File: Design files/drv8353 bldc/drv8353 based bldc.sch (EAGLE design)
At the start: 125 parts, among them IC1 DRV8353RSRGZT, J1 SSQ-110-01-G-D, J2 SSQ-110-01-G-D, J4 B06B-HCMKK

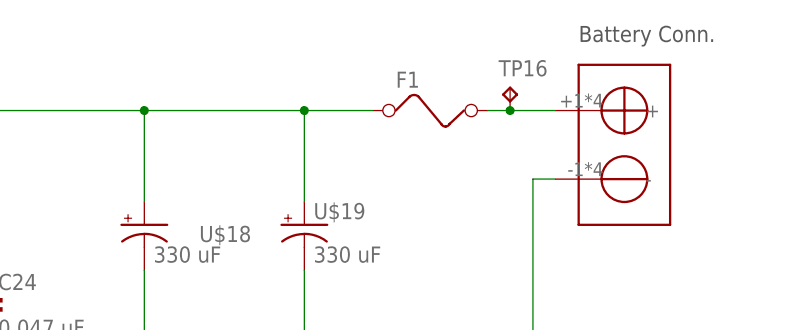
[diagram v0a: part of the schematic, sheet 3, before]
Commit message: replaced generic fuse with automotive style blade fuse
fuse chosen was the maxi standard becasue the regular ATO fuses max out at 40 amps and I'm not sure if that's enough for how we want to fuse this board
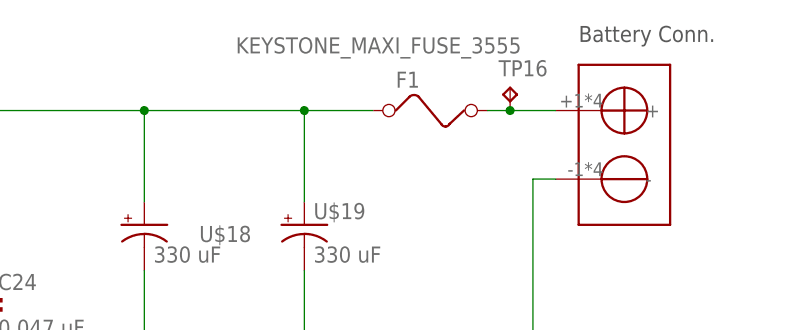
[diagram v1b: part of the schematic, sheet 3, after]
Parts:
- F1: value (none) -> KEYSTONE_MAXI_FUSE_3555; device special:FUSE -> REV BLDC:KEYSTONE_MAXI_FUSE_3555
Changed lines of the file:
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@@
 <part name="U$18" library="REV BLDC" deviceset="RADIALK16" device="" value="330 uF"/>
 <part name="U$19" library="REV BLDC" deviceset="RADIALK16" device="" value="330 uF"/>
-<part name="F1" library="special" library_urn="urn:adsk.eagle:library:367" deviceset="FUSE" device="" package3d_urn="urn:adsk.eagle:package:26650/1"/>
+<part name="F1" library="REV BLDC" deviceset="KEYSTONE_MAXI_FUSE_3555" device=""/>
 <part name="TP16" library="testpad" library_urn="urn:adsk.eagle:library:385" deviceset="TP" device="B1,27" package3d_urn="urn:adsk.eagle:package:27944/2"/>
 <part name="SUPPLY1" library="supply2" library_urn="urn:adsk.eagle:library:372" deviceset="GND" device=""/>
@@
 <instance part="F1" gate="G$1" x="60.96" y="71.12" smashed="yes">
 <attribute name="NAME" x="55.88" y="73.66" size="1.778" layer="95"/>
-<attribute name="VALUE" x="55.88" y="67.31" size="1.778" layer="96"/>
+<attribute name="VALUE" x="38.1" y="77.47" size="1.778" layer="96"/>
 </instance>
 <instance part="TP16" gate="G$1" x="68.58" y="73.66" smashed="yes">

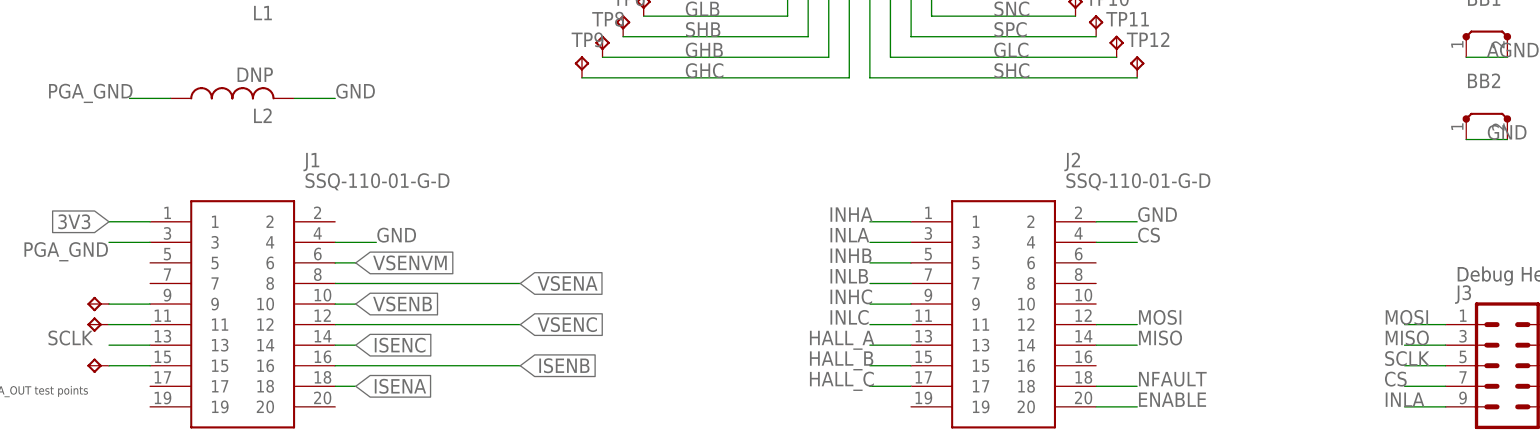
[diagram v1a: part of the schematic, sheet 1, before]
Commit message: created communications boards, combined 2x10 headers
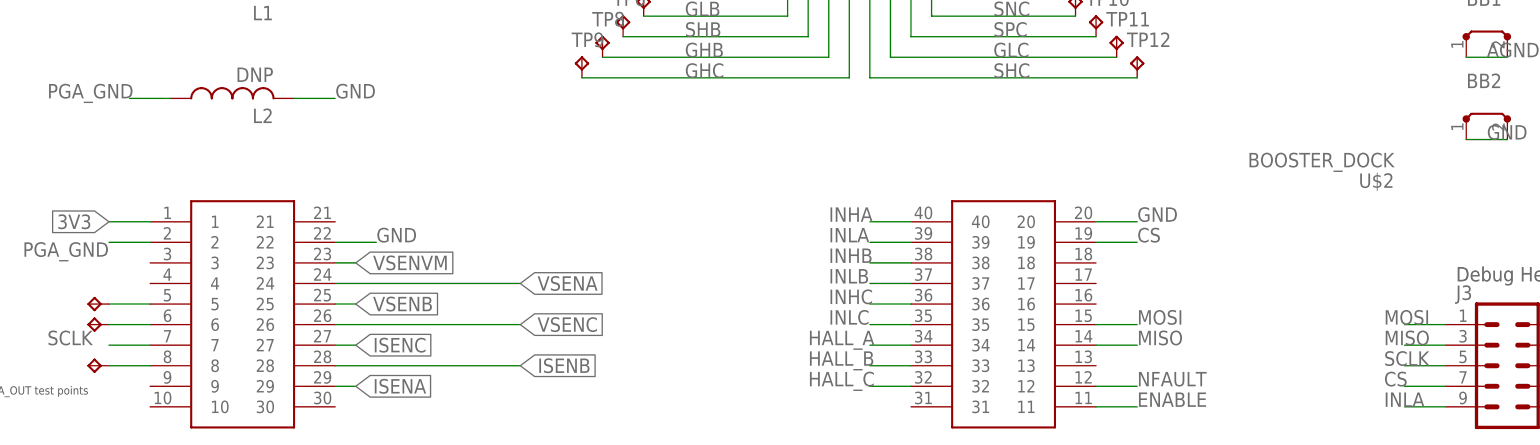
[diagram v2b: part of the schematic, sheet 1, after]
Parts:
- removed J1, J2: SSQ-110-01-G-D, SamacSys_Parts:SSQ-110-01-G-D
- added U$2: BOOSTER_DOCK, REV BLDC:BOOSTER_DOCK
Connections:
- net 3V3: now also U$2.1; no longer J1.1
- net CS: now also U$2.19; no longer J2.4
- net ENABLE: now also U$2.11; no longer J2.20
- net GND: now also U$2.20, U$2.22; no longer J1.4, J2.2
- net HALL_A: now also U$2.34; no longer J2.13
- net HALL_B: now also U$2.33; no longer J2.15
- net HALL_C: now also U$2.32; no longer J2.17
- net INHA: now also U$2.40; no longer J2.1
- net INHB: now also U$2.38; no longer J2.5
- net INHC: now also U$2.36; no longer J2.9
- net INLA: now also U$2.39; no longer J2.3
- net INLB: now also U$2.37; no longer J2.7
- net INLC: now also U$2.35; no longer J2.11
- net ISENA: now also U$2.29; no longer J1.18
- net ISENB: now also U$2.28; no longer J1.16
- net ISENC: now also U$2.27; no longer J1.14
- net MISO: now also U$2.14; no longer J2.14
- net MOSI: now also U$2.15; no longer J2.12
- net N$17: now also U$2.8; no longer J1.15
- net N$18: now also U$2.6; no longer J1.11
- net N$19: now also U$2.5; no longer J1.9
- net NFAULT: now also U$2.12; no longer J2.18
- net PGA_GND: now also U$2.2; no longer J1.3
- net SCLK: now also U$2.7; no longer J1.13
- net VSENA: now also U$2.24; no longer J1.8
- net VSENB: now also U$2.25; no longer J1.10
- net VSENC: now also U$2.26; no longer J1.12
- net VSENVM: now also U$2.23; no longer J1.6

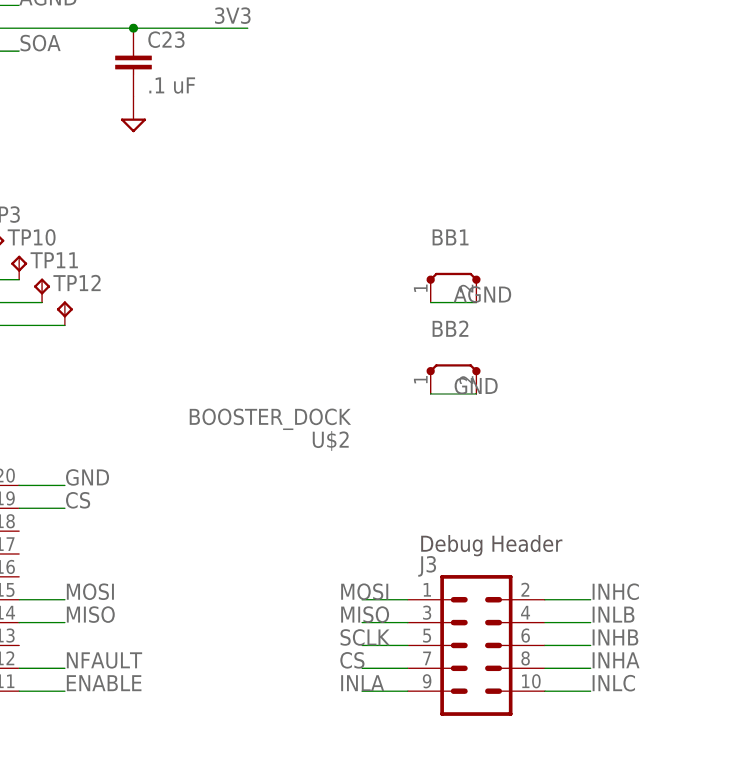
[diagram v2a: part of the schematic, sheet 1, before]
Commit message: adds power switch to motor controller
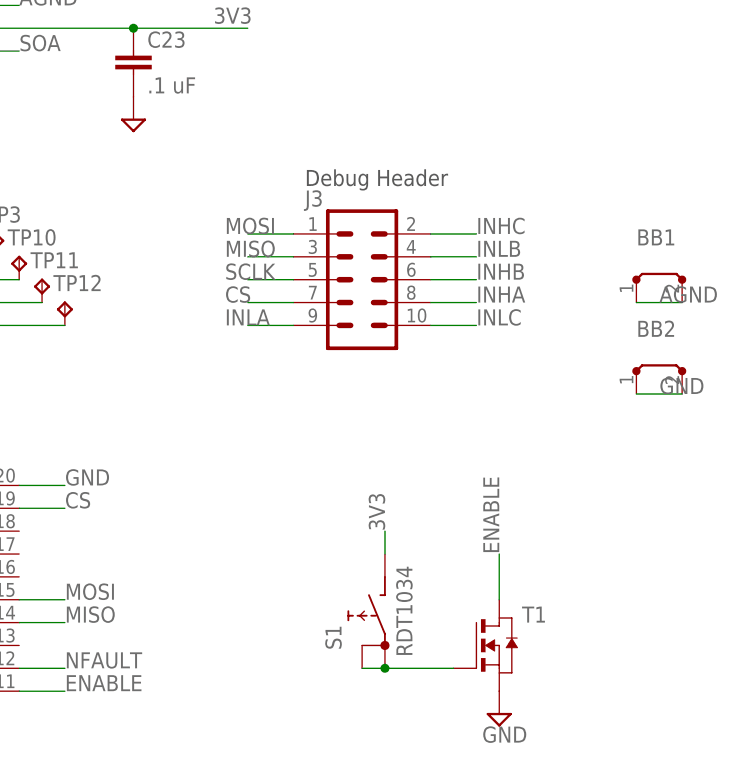
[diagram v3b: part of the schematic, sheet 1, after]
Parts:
- added S1: RDT1034, switch:RDT1034
- added T1: (no value), zetex:NMOSSOT23
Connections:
- new net N$20: S1.A, S1.A1, T1.G
- net 3V3: now also S1.B
- net ENABLE: now also T1.D
- net GND: now also T1.S
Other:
- moved on the sheet: BB1, BB2, J3
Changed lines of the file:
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@@
 <?xml version="1.0" encoding="utf-8"?>
 <!DOCTYPE eagle SYSTEM "eagle.dtd">
-<eagle version="9.5.0">
+<eagle version="9.5.1">
 <drawing>
 <settings>
@@
 <part name="J4" library="SamacSys_Parts" deviceset="B06B-HCMKK" device=""/>
 <part name="U$2" library="REV BLDC" deviceset="BOOSTER_DOCK" device=""/>
+<part name="S1" library="switch" library_urn="urn:adsk.eagle:library:380" deviceset="RDT1034" device="" package3d_urn="urn:adsk.eagle:package:27704/1"/>
+<part name="T1" library="zetex" library_urn="urn:adsk.eagle:library:418" deviceset="NMOSSOT23" device="" package3d_urn="urn:adsk.eagle:package:30981/1"/>
+<part name="SUPPLY10" library="supply2" library_urn="urn:adsk.eagle:library:372" deviceset="GND" device=""/>
 </parts>
 <sheets>
@@
 <plain>
 <frame x1="-96.52" y1="-154.94" x2="134.62" y2="33.02" columns="8" rows="5" layer="97"/>
-<text x="92.71" y="-124.206" size="1.778" layer="97">Debug Header</text>
+<text x="80.01" y="-83.566" size="1.778" layer="97">Debug Header</text>
 <text x="-76.2" y="-137.16" size="1.016" layer="97" rot="R180">PGA_OUT test points</text>
 <text x="-66.04" y="-86.36" size="1.778" layer="97">Ferrite Bead</text>
@@
 <attribute name="TP_SIGNAL_NAME" x="-3.81" y="-59.69" size="1.778" layer="97" rot="R180"/>
 </instance>
-<instance part="J3" gate="G$1" x="99.06" y="-134.62" smashed="yes">
-<attribute name="VALUE" x="95.25" y="-144.526" size="1.778" layer="96" font="vector"/>
-<attribute name="NAME" x="92.71" y="-126.492" size="1.778" layer="95" font="vector"/>
+<instance part="J3" gate="G$1" x="86.36" y="-93.98" smashed="yes">
+<attribute name="VALUE" x="82.55" y="-103.886" size="1.778" layer="96" font="vector"/>
+<attribute name="NAME" x="80.01" y="-85.852" size="1.778" layer="95" font="vector"/>
 </instance>
 <instance part="L2" gate="G$1" x="-58.42" y="-101.6" smashed="yes" rot="R90">
@@
 <attribute name="VALUE" x="-53.34" y="-85.09" size="1.778" layer="96" rot="R180"/>
 </instance>
-<instance part="BB1" gate="1" x="96.52" y="-93.98" smashed="yes">
-<attribute name="NAME" x="93.98" y="-90.17" size="1.778" layer="95"/>
-<attribute name="VALUE" x="93.98" y="-92.71" size="1.778" layer="96"/>
-</instance>
-<instance part="BB2" gate="1" x="96.52" y="-104.14" smashed="yes">
-<attribute name="NAME" x="93.98" y="-100.33" size="1.778" layer="95"/>
-<attribute name="VALUE" x="93.98" y="-102.87" size="1.778" layer="96"/>
-</instance>
-<instance part="U$2" gate="G$1" x="-68.58" y="-116.84" smashed="yes">
-<attribute name="NAME" x="-49.53" y="-109.22" size="1.778" layer="95" align="center-left"/>
-<attribute name="VALUE" x="-49.53" y="-111.76" size="1.778" layer="96" align="center-left"/>
-<attribute name="NAME" x="85.09" y="-111.76" size="1.778" layer="95" rot="R180" align="center-left"/>
-<attribute name="VALUE" x="85.09" y="-109.22" size="1.778" layer="96" rot="R180" align="center-left"/>
+<instance part="BB1" gate="1" x="119.38" y="-93.98" smashed="yes">
+<attribute name="NAME" x="116.84" y="-90.17" size="1.778" layer="95"/>
+<attribute name="VALUE" x="116.84" y="-92.71" size="1.778" layer="96"/>
+</instance>
+<instance part="BB2" gate="1" x="119.38" y="-104.14" smashed="yes">
+<attribute name="NAME" x="116.84" y="-100.33" size="1.778" layer="95"/>
+<attribute name="VALUE" x="116.84" y="-102.87" size="1.778" layer="96"/>
+</instance>
+<instance part="U$2" gate="G$1" x="-68.58" y="-116.84" smashed="yes"/>
+<instance part="S1" gate="G$1" x="86.36" y="-132.08" smashed="yes" rot="R90">
+<attribute name="NAME" x="84.074" y="-135.128" size="1.778" layer="95" rot="R90"/>
+<attribute name="VALUE" x="91.948" y="-135.89" size="1.778" layer="96" rot="R90"/>
+</instance>
+<instance part="T1" gate="A" x="101.6" y="-134.62" smashed="yes">
+<attribute name="VALUE" x="104.14" y="-134.62" size="1.778" layer="96"/>
+<attribute name="NAME" x="104.14" y="-132.08" size="1.778" layer="95"/>
+</instance>
+<instance part="SUPPLY10" gate="GND" x="101.6" y="-142.24" smashed="yes">
+<attribute name="VALUE" x="99.695" y="-145.415" size="1.778" layer="96"/>
 </instance>
 </instances>
@@
 <pinref part="BB2" gate="1" pin="P@1"/>
 <pinref part="BB2" gate="1" pin="P@2"/>
-<wire x1="93.98" y1="-106.68" x2="99.06" y2="-106.68" width="0.1524" layer="91"/>
-<label x="96.52" y="-106.68" size="1.778" layer="95"/>
+<wire x1="116.84" y1="-106.68" x2="121.92" y2="-106.68" width="0.1524" layer="91"/>
+<label x="119.38" y="-106.68" size="1.778" layer="95"/>
 </segment>
 <segment>
@@
 <label x="53.34" y="-116.84" size="1.778" layer="95"/>
 <pinref part="U$2" gate="G$1" pin="20"/>
+</segment>
+<segment>
+<pinref part="T1" gate="A" pin="S"/>
+<pinref part="SUPPLY10" gate="GND" pin="GND"/>
 </segment>
 </net>
@@
 <segment>
 <pinref part="J3" gate="G$1" pin="4"/>
-<wire x1="106.68" y1="-132.08" x2="111.76" y2="-132.08" width="0.1524" layer="91"/>
-<label x="111.76" y="-132.08" size="1.778" layer="95"/>
+<wire x1="93.98" y1="-91.44" x2="99.06" y2="-91.44" width="0.1524" layer="91"/>
+<label x="99.06" y="-91.44" size="1.778" layer="95"/>
 </segment>
 </net>
@@
 <segment>
 <pinref part="J3" gate="G$1" pin="2"/>
-<wire x1="106.68" y1="-129.54" x2="111.76" y2="-129.54" width="0.1524" layer="91"/>
-<label x="111.76" y="-129.54" size="1.778" layer="95"/>
+<wire x1="93.98" y1="-88.9" x2="99.06" y2="-88.9" width="0.1524" layer="91"/>
+<label x="99.06" y="-88.9" size="1.778" layer="95"/>
 </segment>
 </net>
@@
 <segment>
 <pinref part="J3" gate="G$1" pin="10"/>
-<wire x1="106.68" y1="-139.7" x2="111.76" y2="-139.7" width="0.1524" layer="91"/>
-<label x="111.76" y="-139.7" size="1.778" layer="95"/>
+<wire x1="93.98" y1="-99.06" x2="99.06" y2="-99.06" width="0.1524" layer="91"/>
+<label x="99.06" y="-99.06" size="1.778" layer="95"/>
 </segment>
 </net>
@@
 <segment>
 <pinref part="J3" gate="G$1" pin="6"/>
-<wire x1="106.68" y1="-134.62" x2="111.76" y2="-134.62" width="0.1524" layer="91"/>
-<label x="111.76" y="-134.62" size="1.778" layer="95"/>
+<wire x1="93.98" y1="-93.98" x2="99.06" y2="-93.98" width="0.1524" layer="91"/>
+<label x="99.06" y="-93.98" size="1.778" layer="95"/>
 </segment>
 </net>
@@
 <segment>
 <pinref part="J3" gate="G$1" pin="9"/>
-<wire x1="91.44" y1="-139.7" x2="86.36" y2="-139.7" width="0.1524" layer="91"/>
-<label x="83.82" y="-139.7" size="1.778" layer="95"/>
+<wire x1="78.74" y1="-99.06" x2="73.66" y2="-99.06" width="0.1524" layer="91"/>
+<label x="71.12" y="-99.06" size="1.778" layer="95"/>
 </segment>
 </net>
@@
 <segment>
 <pinref part="J3" gate="G$1" pin="8"/>
-<wire x1="106.68" y1="-137.16" x2="111.76" y2="-137.16" width="0.1524" layer="91"/>
-<label x="111.76" y="-137.16" size="1.778" layer="95"/>
+<wire x1="93.98" y1="-96.52" x2="99.06" y2="-96.52" width="0.1524" layer="91"/>
+<label x="99.06" y="-96.52" size="1.778" layer="95"/>
 </segment>
 </net>
@@
 <pinref part="U$2" gate="G$1" pin="1"/>
 </segment>
+<segment>
+<pinref part="S1" gate="G$1" pin="B"/>
+<wire x1="88.9" y1="-124.46" x2="88.9" y2="-121.92" width="0.1524" layer="91"/>
+<label x="88.9" y="-121.92" size="1.778" layer="95" rot="R90"/>
+</segment>
 </net>
 <net name="ENABLE" class="0">
@@
 <pinref part="U$2" gate="G$1" pin="11"/>
 </segment>
+<segment>
+<pinref part="T1" gate="A" pin="D"/>
+<wire x1="101.6" y1="-129.54" x2="101.6" y2="-124.46" width="0.1524" layer="91"/>
+<label x="101.6" y="-124.46" size="1.778" layer="95" rot="R90"/>
+</segment>
 </net>
 <net name="CS" class="0">
@@
 <segment>
 <pinref part="J3" gate="G$1" pin="7"/>
-<wire x1="91.44" y1="-137.16" x2="86.36" y2="-137.16" width="0.1524" layer="91"/>
-<label x="83.82" y="-137.16" size="1.778" layer="95"/>
+<wire x1="78.74" y1="-96.52" x2="73.66" y2="-96.52" width="0.1524" layer="91"/>
+<label x="71.12" y="-96.52" size="1.778" layer="95"/>
 </segment>
 <segment>
@@
 <segment>
 <pinref part="J3" gate="G$1" pin="5"/>
-<wire x1="91.44" y1="-134.62" x2="86.36" y2="-134.62" width="0.1524" layer="91"/>
-<label x="83.82" y="-134.62" size="1.778" layer="95"/>
+<wire x1="78.74" y1="-93.98" x2="73.66" y2="-93.98" width="0.1524" layer="91"/>
+<label x="71.12" y="-93.98" size="1.778" layer="95"/>
 </segment>
 </net>
@@
 <segment>
 <pinref part="J3" gate="G$1" pin="1"/>
-<wire x1="91.44" y1="-129.54" x2="86.36" y2="-129.54" width="0.1524" layer="91"/>
-<label x="83.82" y="-129.54" size="1.778" layer="95"/>
+<wire x1="78.74" y1="-88.9" x2="73.66" y2="-88.9" width="0.1524" layer="91"/>
+<label x="71.12" y="-88.9" size="1.778" layer="95"/>
 </segment>
 </net>
@@
 <segment>
 <pinref part="J3" gate="G$1" pin="3"/>
-<wire x1="91.44" y1="-132.08" x2="86.36" y2="-132.08" width="0.1524" layer="91"/>
-<label x="83.82" y="-132.08" size="1.778" layer="95"/>
+<wire x1="78.74" y1="-91.44" x2="73.66" y2="-91.44" width="0.1524" layer="91"/>
+<label x="71.12" y="-91.44" size="1.778" layer="95"/>
 </segment>
 </net>
@@
 <pinref part="BB1" gate="1" pin="P@1"/>
 <pinref part="BB1" gate="1" pin="P@2"/>
-<wire x1="93.98" y1="-96.52" x2="99.06" y2="-96.52" width="0.1524" layer="91"/>
-<label x="96.52" y="-96.52" size="1.778" layer="95"/>
+<wire x1="116.84" y1="-96.52" x2="121.92" y2="-96.52" width="0.1524" layer="91"/>
+<label x="119.38" y="-96.52" size="1.778" layer="95"/>
 </segment>
 </net>
@@
 </segment>
 </net>
+<net name="N$20" class="0">
+<segment>
+<pinref part="S1" gate="G$1" pin="A1"/>
+<pinref part="S1" gate="G$1" pin="A"/>
+<wire x1="88.9" y1="-137.16" x2="86.36" y2="-137.16" width="0.1524" layer="91"/>
+<pinref part="T1" gate="A" pin="G"/>
+<wire x1="96.52" y1="-137.16" x2="88.9" y2="-137.16" width="0.1524" layer="91"/>
+<junction x="88.9" y="-137.16"/>
+</segment>
+</net>

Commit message: adds header to select between battery and buck supply for VM
can also be used to power VM off external supply
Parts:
- added SV1: (no value), con-lstb:MA03-1
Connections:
- new net DRV_VM: C25.1, C26.1, IC1.VM, SV1.2, TP15.TP
- net VBUCK: now also SV1.1; no longer C25.1, C26.1, IC1.VM, TP15.TP
- net VM: now also SV1.3
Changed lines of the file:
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@@
 <?xml version="1.0" encoding="utf-8"?>
 <!DOCTYPE eagle SYSTEM "eagle.dtd">
-<eagle version="9.5.1">
+<eagle version="9.5.0">
 <drawing>
 <settings>
@@
 <part name="T1" library="zetex" library_urn="urn:adsk.eagle:library:418" deviceset="NMOSSOT23" device="" package3d_urn="urn:adsk.eagle:package:30981/1"/>
 <part name="SUPPLY10" library="supply2" library_urn="urn:adsk.eagle:library:372" deviceset="GND" device=""/>
+<part name="SV1" library="con-lstb" library_urn="urn:adsk.eagle:library:162" deviceset="MA03-1" device="" package3d_urn="urn:adsk.eagle:package:8339/1"/>
 </parts>
 <sheets>
@@
 <attribute name="VALUE" x="99.695" y="-145.415" size="1.778" layer="96"/>
 </instance>
+<instance part="SV1" gate="G$1" x="-68.58" y="-50.8" smashed="yes">
+<attribute name="VALUE" x="-69.85" y="-58.42" size="1.778" layer="96"/>
+<attribute name="NAME" x="-69.85" y="-44.958" size="1.778" layer="95"/>
+</instance>
 </instances>
 <busses>
@@
 <wire x1="-2.54" y1="0" x2="-7.62" y2="0" width="0.1524" layer="91"/>
 <label x="-10.16" y="0" size="1.778" layer="95"/>
+</segment>
+<segment>
+<pinref part="SV1" gate="G$1" pin="3"/>
+<wire x1="-60.96" y1="-48.26" x2="-53.34" y2="-48.26" width="0.1524" layer="91"/>
+<label x="-60.96" y="-48.26" size="1.778" layer="95"/>
 </segment>
 </net>
@@
 </segment>
 <segment>
-<pinref part="IC1" gate="G$1" pin="VM"/>
-<wire x1="-2.54" y1="-50.8" x2="-35.56" y2="-50.8" width="0.1524" layer="91"/>
-<label x="-58.42" y="-52.832" size="1.778" layer="95"/>
-<pinref part="C26" gate="G$1" pin="1"/>
-<wire x1="-35.56" y1="-50.8" x2="-43.18" y2="-50.8" width="0.1524" layer="91"/>
-<wire x1="-43.18" y1="-53.34" x2="-43.18" y2="-50.8" width="0.1524" layer="91"/>
-<junction x="-43.18" y="-50.8"/>
-<pinref part="C25" gate="G$1" pin="1"/>
-<wire x1="-35.56" y1="-53.34" x2="-35.56" y2="-50.8" width="0.1524" layer="91"/>
-<junction x="-35.56" y="-50.8"/>
-<junction x="-48.26" y="-50.8"/>
-<wire x1="-43.18" y1="-50.8" x2="-48.26" y2="-50.8" width="0.1524" layer="91"/>
-<pinref part="TP15" gate="G$1" pin="TP"/>
-<wire x1="-48.26" y1="-50.8" x2="-53.34" y2="-50.8" width="0.1524" layer="91"/>
+<pinref part="SV1" gate="G$1" pin="1"/>
+<wire x1="-60.96" y1="-53.34" x2="-53.34" y2="-53.34" width="0.1524" layer="91"/>
+<label x="-60.96" y="-55.88" size="1.778" layer="95"/>
 </segment>
 </net>
@@
 </segment>
 </net>
+<net name="DRV_VM" class="0">
+<segment>
+<pinref part="IC1" gate="G$1" pin="VM"/>
+<pinref part="SV1" gate="G$1" pin="2"/>
+<wire x1="-2.54" y1="-50.8" x2="-35.56" y2="-50.8" width="0.1524" layer="91"/>
+<pinref part="TP15" gate="G$1" pin="TP"/>
+<wire x1="-35.56" y1="-50.8" x2="-43.18" y2="-50.8" width="0.1524" layer="91"/>
+<wire x1="-43.18" y1="-50.8" x2="-48.26" y2="-50.8" width="0.1524" layer="91"/>
+<wire x1="-48.26" y1="-50.8" x2="-60.96" y2="-50.8" width="0.1524" layer="91"/>
+<junction x="-48.26" y="-50.8"/>
+<pinref part="C26" gate="G$1" pin="1"/>
+<wire x1="-43.18" y1="-53.34" x2="-43.18" y2="-50.8" width="0.1524" layer="91"/>
+<junction x="-43.18" y="-50.8"/>
+<pinref part="C25" gate="G$1" pin="1"/>
+<wire x1="-35.56" y1="-53.34" x2="-35.56" y2="-50.8" width="0.1524" layer="91"/>
+<junction x="-35.56" y="-50.8"/>
+<label x="-60.96" y="-50.8" size="1.778" layer="95"/>
+</segment>
+</net>
